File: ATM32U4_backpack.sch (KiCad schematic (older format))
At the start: 39 parts, among them J1 ISP, J2 WS2812, J3 UART, J4 USB_B_Micro, J5 OLED, J6 ENC, U1 LM3480-3.3, U3 NTS0101GW, U4 ATmega32U4-AU, Y1 16MHz

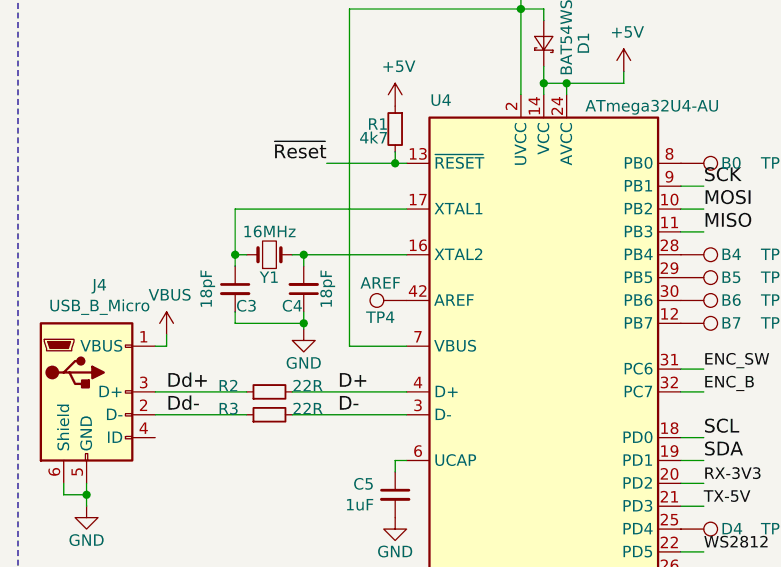
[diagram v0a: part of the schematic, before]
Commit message: Fixed back silkscreen
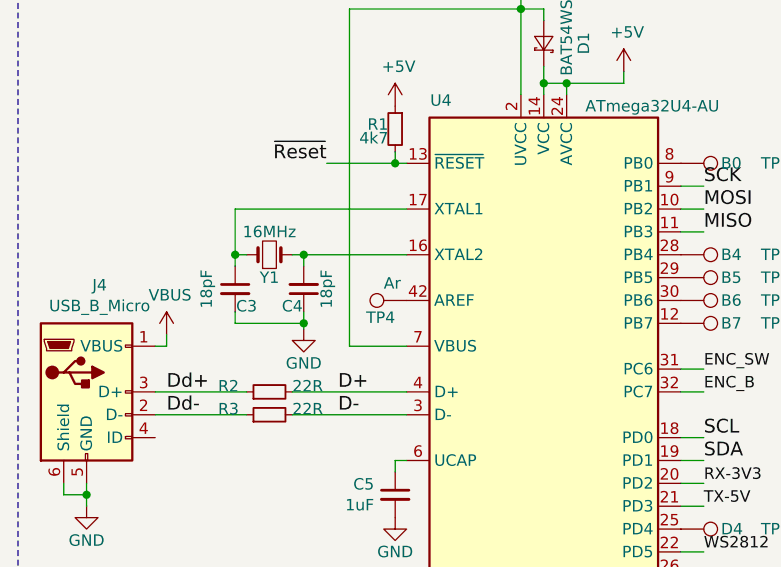
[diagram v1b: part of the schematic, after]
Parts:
- TP4: value AREF -> Ar
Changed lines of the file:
@@
 P 3275 2200
 F 0 "TP4" V 3200 2250 50  0000 L CNN
-F 1 "AREF" V 3350 2225 50  0000 L CNN
+F 1 "Ar" V 3350 2225 50  0000 L CNN
 F 2 "TestPoint:TestPoint_Pad_1.0x1.0mm" H 3475 2200 50  0001 C CNN
 F 3 "~" H 3475 2200 50  0001 C CNN

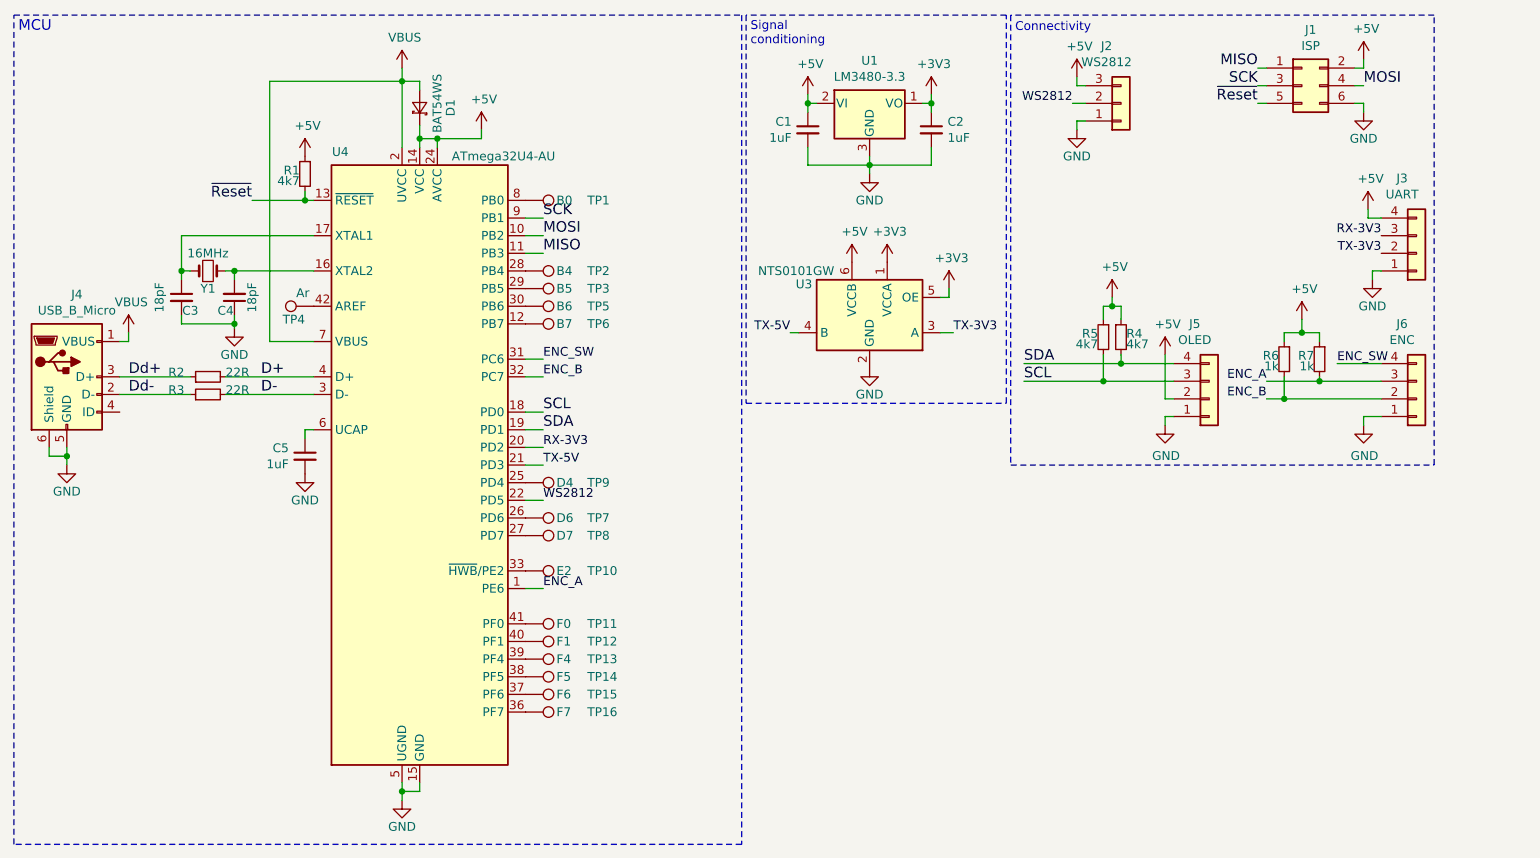
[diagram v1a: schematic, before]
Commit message: Made SPI level-shifted to 3v3
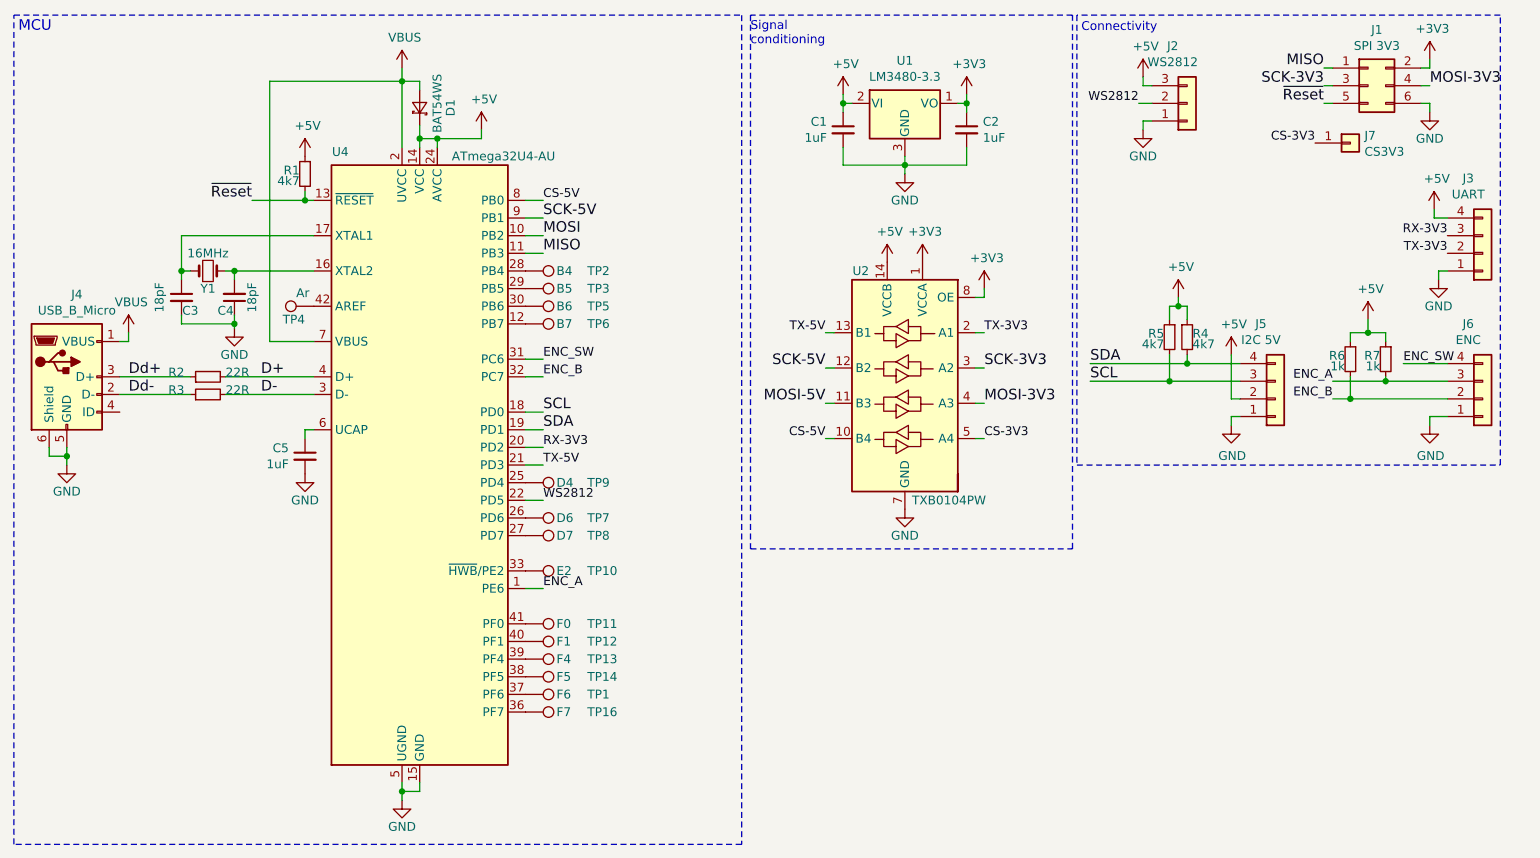
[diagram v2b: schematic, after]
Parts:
- removed TP15: F6, TestPoint:TestPoint_Pad_1.0x1.0mm, symbol Connector:TestPoint
- removed U3: NTS0101GW, Package_TO_SOT_SMD:SOT-363_SC-70-6, symbol Logic_LevelTranslator:NTS0101GW
- added J7: CS3V3, Connector_PinHeader_2.54mm:PinHeader_1x01_P2.54mm_Horizontal, symbol Connector_Generic:Conn_01x01
- added U2: TXB0104PW, Package_SO:TSSOP-14_4.4x5mm_P0.65mm, symbol Logic_LevelTranslator:TXB0104PW
- J1: value ISP -> SPI 3V3
- J5: value OLED -> I2C 5V
- TP1: value B0 -> F6
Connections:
- net +3V3: now also J1.2 (Pin_2), U2.1 (VCCA), U2.8 (OE)
- net +5V: now also U2.14 (VCCB); no longer J1.2 (Pin_2)
- net GND: now also U2.7 (GND)
- net MOSI: no longer J1.4 (Pin_4)
- net TX-3V3: now also U2.2 (A1)
- net TX-5V: now also U2.13 (B1)
- net at U4.37 (PF6): now also TP1.1
- net CS-5V: now reaches U4.8 (PB0)
- net CS-5V: now also U2.10 (B4); no longer TP1.1
- net SCK renamed SCK-3V3
- net SCK-3V3: now also U2.3 (A2); no longer U4.9 (PB1)
- new net CS-3V3: J7.1 (Pin_1), U2.5 (A4)
- new net MOSI-3V3: J1.4 (Pin_4), U2.4 (A3)
- new net MOSI-5V: U2.11 (B3)
- new net SCK-5V: U2.12 (B2), U4.9 (PB1)
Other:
- moved on the sheet: C1, C2, J1, J2, J3, J5, J6, R4, R5, R6, R7, TP1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
